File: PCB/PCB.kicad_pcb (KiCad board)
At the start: 2 copper layers, 110 x 100 mm, 54 parts, among them J1 Conn_01x03, J2 Conn_01x02, Q1 2N2907, Q10 TIP32, Q11 BD138, Q12 TIP31, Q13 2N2222, Q2 2N2907, Q3 2N2907, Q4 2N2222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

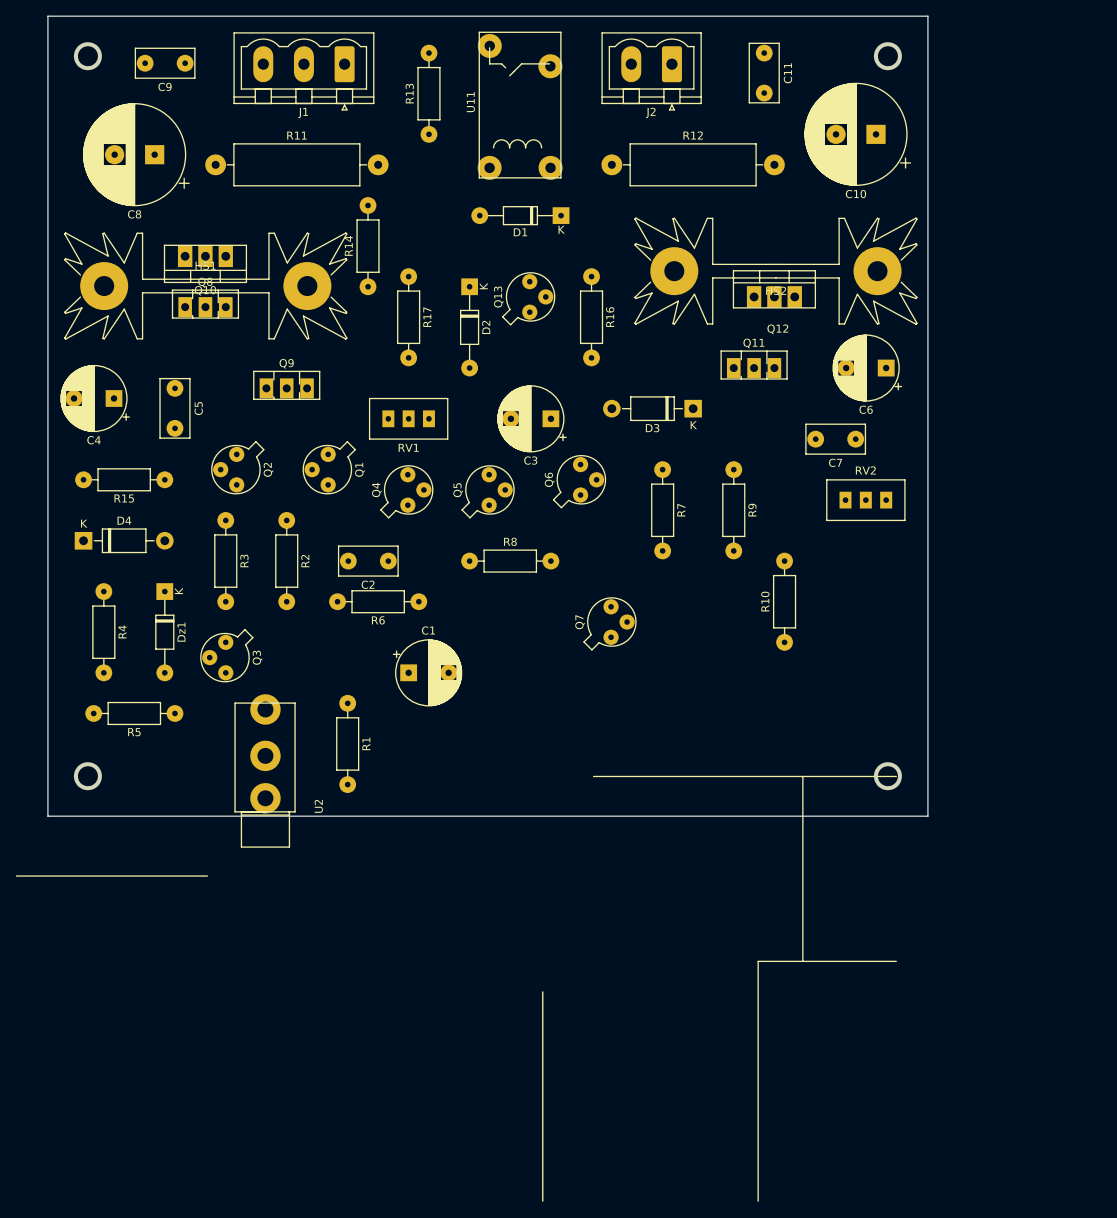
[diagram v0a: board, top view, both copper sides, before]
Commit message: placement rereterminé
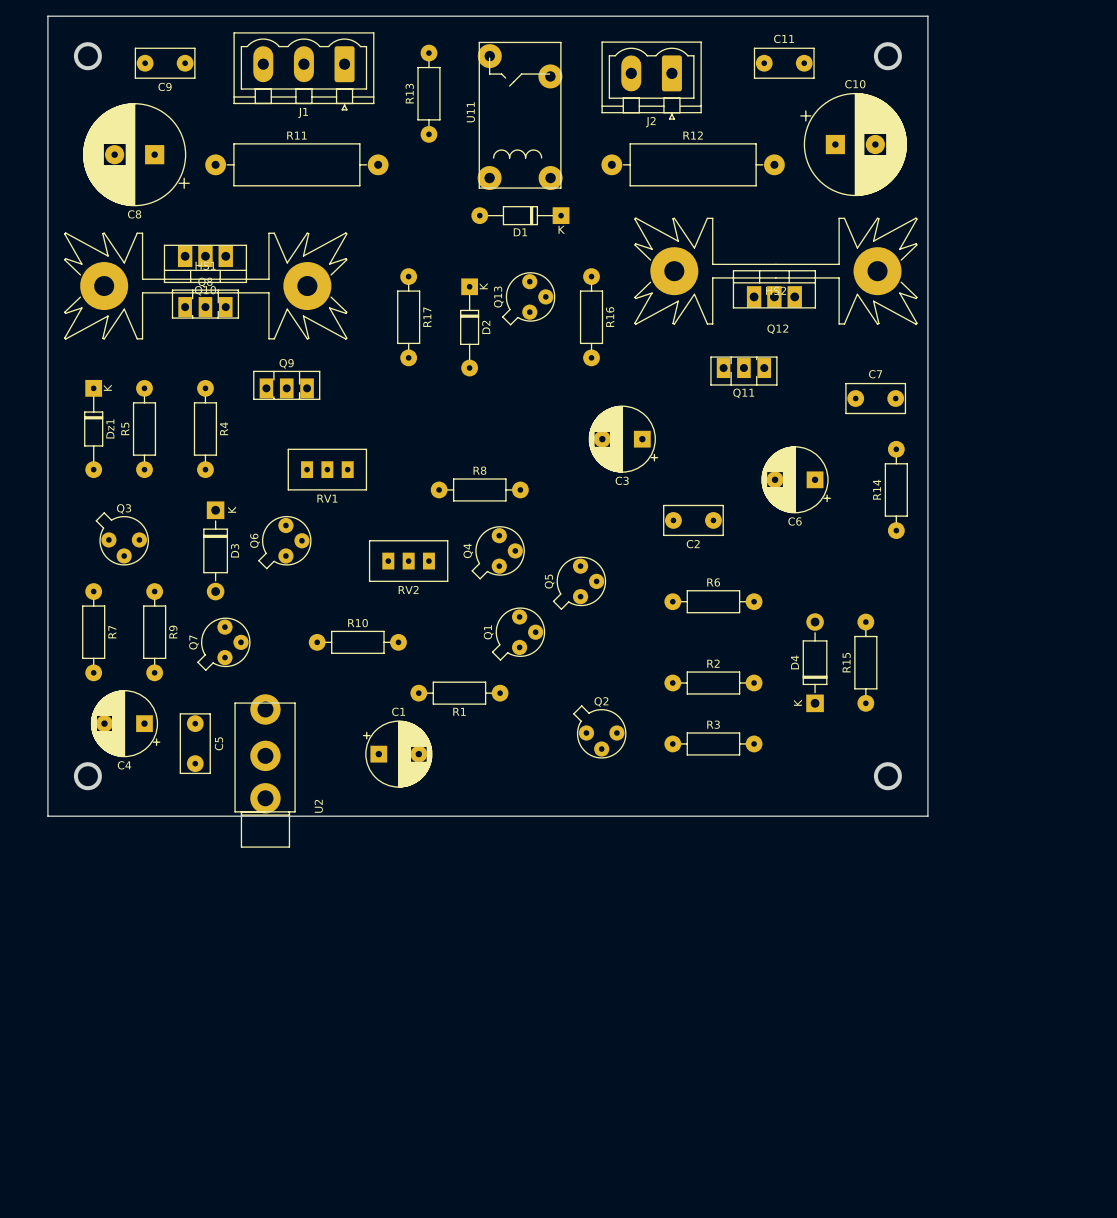
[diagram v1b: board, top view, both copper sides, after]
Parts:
- moved D4 93.7 mm to (135.9, 135.9), turned to 90 degrees
- moved R15 92.0 mm to (142.2, 135.9), turned to 90 degrees
- moved R9 74.0 mm to (53.3, 121.9)
- moved R14 72.7 mm to (146.1, 114.3)
- moved R7 72.7 mm to (45.7, 121.9)
- moved RV2 62.7 mm to (82.5, 118.1), turned to 180 degrees
- moved R3 62.5 mm to (118.1, 141.0), turned to 0 degrees
- moved D3 61.0 mm to (61.0, 111.8), turned to 270 degrees
- moved R10 58.4 mm to (73.7, 128.3), turned to 0 degrees
- moved Q2 56.1 mm to (108.0, 139.7), turned to 0 degrees
- moved R2 52.4 mm to (118.1, 133.3), turned to 0 degrees
- moved Q7 48.3 mm to (62.2, 129.5)
- moved C5 42.0 mm to (58.4, 138.4)
- moved C2 41.0 mm to (123.2, 113.0)
- moved C4 40.8 mm to (52.1, 138.4)
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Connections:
- J2 pad 1: Net-(J2-Pad1) -> GND
- J2 pad 2: GND -> Net-(J2-Pad1)

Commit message: nulnulnul
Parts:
- moved R5 24.7 mm to (76.2, 101.6), turned to 0 degrees
- moved R14 24.7 mm to (170.2, 109.2)
- moved D4 21.6 mm to (137.2, 114.3), turned to 270 degrees
- moved D3 19.4 mm to (44.5, 121.9)
- moved R15 19.1 mm to (143.5, 116.8)
- moved C7 14.9 mm to (127.0, 92.7)
- moved R7 14.0 mm to (59.7, 121.9)
- moved C2 8.89 mm to (114.3, 113.0)
- moved Q7 7.73 mm to (69.8, 130.8)
- moved Q6 7.41 mm to (76.2, 120.7)
- moved R10 6.84 mm to (80.0, 130.8)
- moved Q3 5.72 mm to (54.0, 115.5), turned to 180 degrees
- moved C3 5.68 mm to (119.4, 105.4), turned to 0 degrees
- moved R3 5.68 mm to (123.2, 143.5)
- moved R2 5.68 mm to (120.7, 128.3), turned to 270 degrees
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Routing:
- net GND: track 0.00 -> 292.7 mm
- net -12V: track 0.00 -> 216.9 mm
- net +12V: track 0.00 -> 195.8 mm
- net Net-(C2-Pad1): track 0.00 -> 116.3 mm
- net Net-(Q2-Pad2): track 0.00 -> 56.1 mm
- net Net-(Q10-Pad2): track 0.00 -> 47.8 mm
- net Net-(D1-Pad2): track 0.00 -> 45.5 mm
- net Net-(Q6-Pad3): track 0.00 -> 44.5 mm
- net Net-(Dz1-Pad2): track 0.00 -> 43.1 mm
- net Net-(R11-Pad2): track 0.00 -> 40.7 mm
- net Net-(Q10-Pad1): track 0.00 -> 39.3 mm
- net Net-(C2-Pad2): track 0.00 -> 38.1 mm
- net Net-(Q8-Pad3): track 0.00 -> 33.8 mm
- net Net-(C3-Pad1): track 0.00 -> 33.2 mm
- net Net-(C1-Pad1): track 0.00 -> 29.3 mm
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
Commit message: routage terminé
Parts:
- moved R14 47.0 mm to (141.0, 72.4), turned to 180 degrees
- moved C10 2.84 mm to (137.2, 63.5)
- moved C11 2.84 mm to (127.0, 54.6)
- moved R12 1.27 mm to (110.5, 67.3)
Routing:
- net GND: track 292.7 -> 490.7 mm
- net Net-(Q1-Pad1): track 13.1 -> 87.0 mm, vias 0 -> 2
- net Net-(Q2-Pad2): track 56.1 -> 111.3 mm
- net -12V: track 216.9 -> 187.2 mm
- net Net-(C1-Pad2): track 14.3 -> 29.4 mm
- net Net-(R11-Pad2): track 40.7 -> 55.2 mm, vias 0 -> 2
- net Net-(Q6-Pad1): track 20.9 -> 29.8 mm
- net +12V: track 195.8 -> 203.9 mm
- net Net-(Q11-Pad1): track 28.3 -> 32.7 mm
